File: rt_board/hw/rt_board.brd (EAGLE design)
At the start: 100 x 80 mm, 65 parts, among them IC1 MCP170333MB, IC2/L1 TLE4935L, IC3/L1 TLE4935L, IC4/L1 TLE4935L, IC5/L1 TLE4935L, Q1 8MHz, SW1 B3U-1000PM-B, SW2 B3U-1000PM-B, U1 DRV8801PWP, U2 DRV8801PWP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

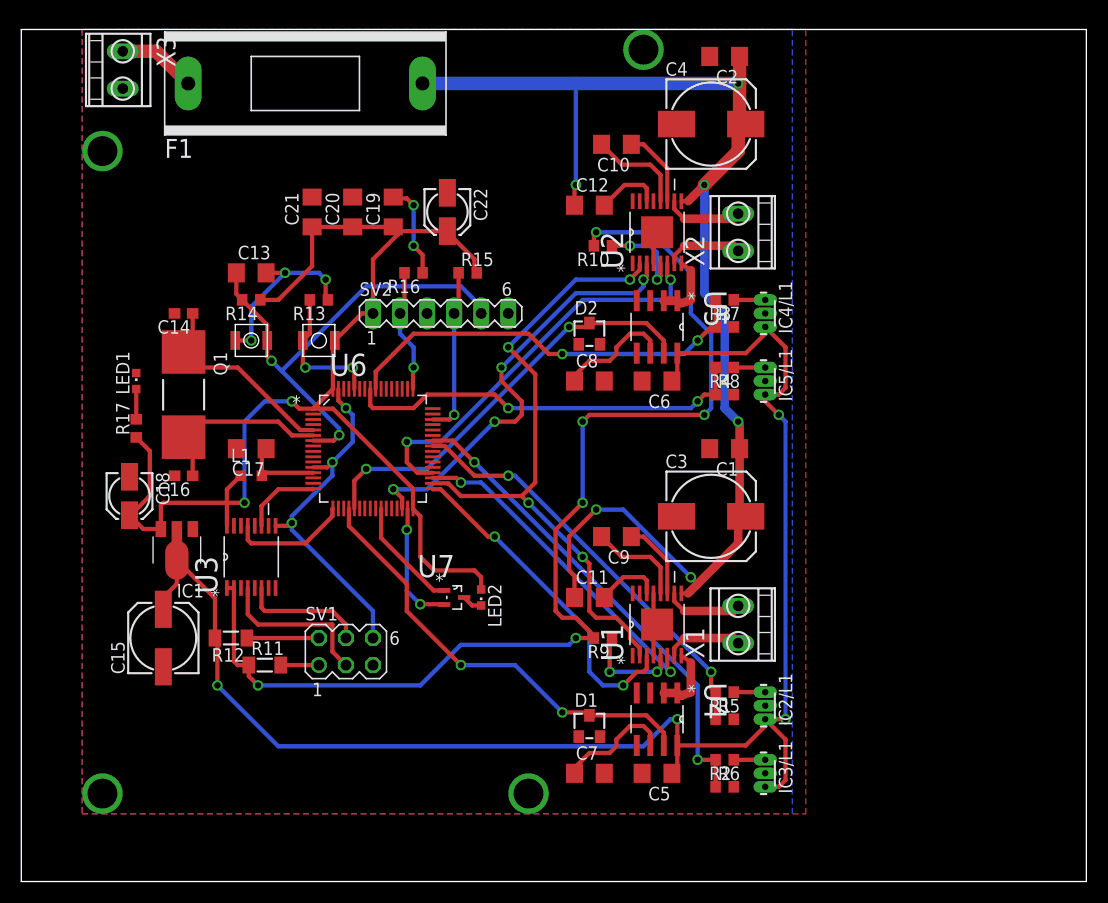
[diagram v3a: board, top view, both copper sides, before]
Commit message: board size optimized; added basic markings what is what
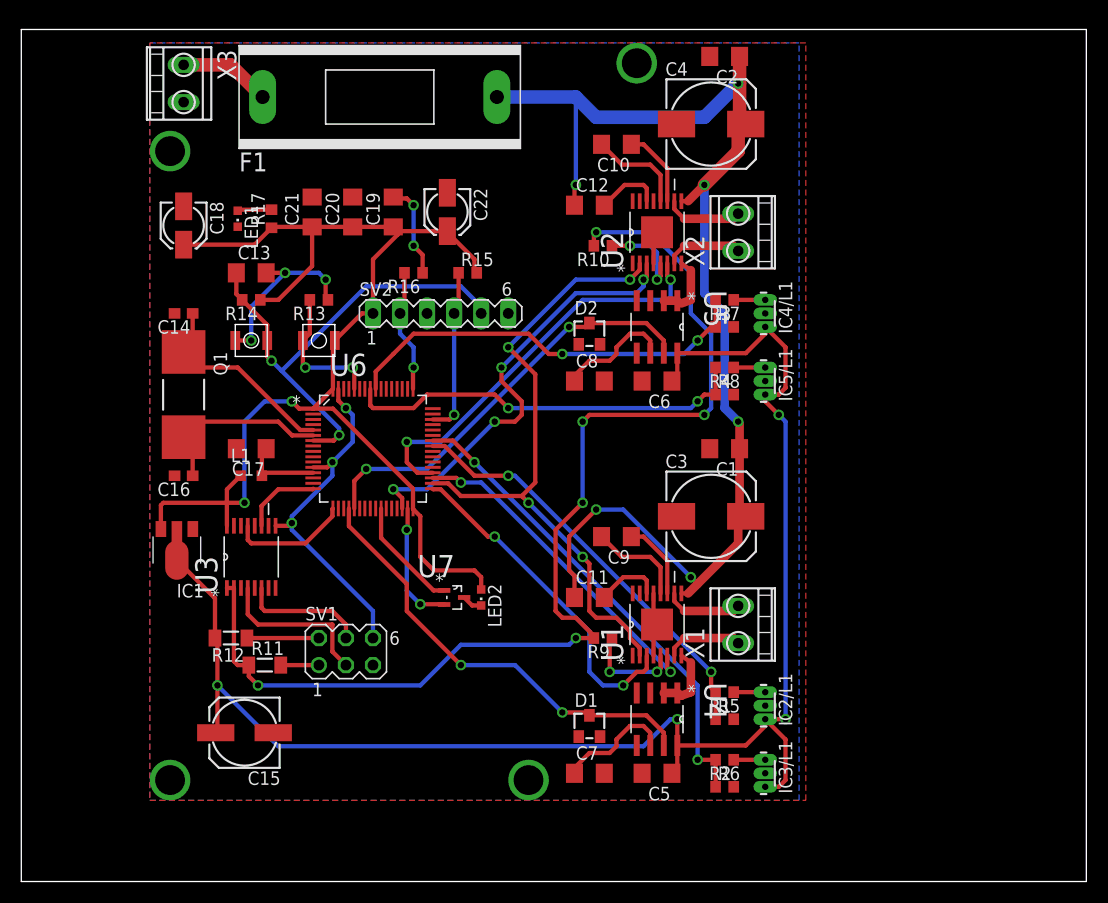
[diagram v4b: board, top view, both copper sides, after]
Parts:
- moved C18 25.9 mm to (15.2, 61.6)
- moved R17 23.4 mm to (23.5, 62.2)
- moved LED1 18.0 mm to (20.3, 62.2), turned to 180 degrees
- moved C15 11.7 mm to (21.0, 14.0), turned to 180 degrees
- moved F1 7.10 mm to (33.7, 73.7)
- moved X3 5.85 mm to (15.2, 74.9)
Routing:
- net +12V: track 124.0 -> 117.8 mm
- net N$2: track 7.40 -> 8.67 mm
- net +5V: track 117.9 -> 118.5 mm
- net +5V/1: track 143.0 -> 142.5 mm
- net 0V: vias 10 -> 14
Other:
- board text added: "+12V"
- board text added: "FASE FUSE 8A"
- board text added: "TIGER RT board v1.0.0-rc1"
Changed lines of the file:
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@@
 <wire x1="100" y1="80" x2="0" y2="80" width="0" layer="20"/>
 <wire x1="0" y1="80" x2="0" y2="0" width="0" layer="20"/>
+<text x="42.545" y="73.025" size="1.778" layer="26" rot="MR0">FASE FUSE 8A</text>
+<text x="16.51" y="71.755" size="1.778" layer="26" rot="MR90">+12V</text>
+<text x="48.895" y="13.335" size="1.778" layer="26" rot="MR0">TIGER RT board v1.0.0-rc1</text>
 </plain>
 <attributes>
@@
 <element name="C19" library="rcl" package="C1206" value="100nF" x="34.925" y="62.865" rot="R90"/>
 <element name="C22" library="rcl" package="153CLV-0405" value="4.7uF" x="40.005" y="62.865" rot="R270"/>
-<element name="C15" library="rcl" package="153CLV-0605" value="100uF" x="13.335" y="22.86" rot="R90"/>
-<element name="C18" library="rcl" package="153CLV-0405" value="4.7uF" x="10.16" y="36.195" rot="R270"/>
-<element name="X3" library="con-ptr500" package="AK550/2" value="PWR" x="9.525" y="76.2" rot="R270">
-<attribute name="OC_NEWARK" value="unknown" x="9.525" y="76.2" size="1.778" layer="27" rot="R270" display="off"/>
-<attribute name="MPN" value="" x="9.525" y="76.2" size="1.778" layer="27" rot="R270" display="off"/>
-<attribute name="MF" value="" x="9.525" y="76.2" size="1.778" layer="27" rot="R270" display="off"/>
-<attribute name="OC_FARNELL" value="unknown" x="9.525" y="76.2" size="1.778" layer="27" rot="R270" display="off"/>
-</element>
-<element name="F1" library="fuse" package="SH22" value="TF8A" x="26.67" y="74.93">
-<attribute name="OC_NEWARK" value="unknown" x="26.67" y="74.93" size="1.778" layer="27" display="off"/>
-<attribute name="MPN" value="" x="26.67" y="74.93" size="1.778" layer="27" display="off"/>
-<attribute name="MF" value="" x="26.67" y="74.93" size="1.778" layer="27" display="off"/>
-<attribute name="OC_FARNELL" value="unknown" x="26.67" y="74.93" size="1.778" layer="27" display="off"/>
+<element name="C15" library="rcl" package="153CLV-0605" value="100uF" x="20.955" y="13.97" rot="R180"/>
+<element name="C18" library="rcl" package="153CLV-0405" value="4.7uF" x="15.24" y="61.595" rot="R270"/>
+<element name="X3" library="con-ptr500" package="AK550/2" value="PWR" x="15.24" y="74.93" rot="R270">
+<attribute name="OC_NEWARK" value="unknown" x="15.24" y="74.93" size="1.778" layer="27" rot="R270" display="off"/>
+<attribute name="MPN" value="" x="15.24" y="74.93" size="1.778" layer="27" rot="R270" display="off"/>
+<attribute name="MF" value="" x="15.24" y="74.93" size="1.778" layer="27" rot="R270" display="off"/>
+<attribute name="OC_FARNELL" value="unknown" x="15.24" y="74.93" size="1.778" layer="27" rot="R270" display="off"/>
+</element>
+<element name="F1" library="fuse" package="SH22" value="TF8A" x="33.655" y="73.66">
+<attribute name="OC_NEWARK" value="unknown" x="33.655" y="73.66" size="1.778" layer="27" display="off"/>
+<attribute name="MPN" value="" x="33.655" y="73.66" size="1.778" layer="27" display="off"/>
+<attribute name="MF" value="" x="33.655" y="73.66" size="1.778" layer="27" display="off"/>
+<attribute name="OC_FARNELL" value="unknown" x="33.655" y="73.66" size="1.778" layer="27" display="off"/>
 </element>
 <element name="C20" library="rcl" package="C1206" value="100nF" x="31.115" y="62.865" rot="R90"/>
@@
 <element name="C12" library="rcl" package="C1206" value="100nF" x="53.34" y="63.5"/>
 <element name="C10" library="rcl" package="C1206" value="100nF" x="55.88" y="69.215" rot="R180"/>
-<element name="LED1" library="led" package="CHIPLED_0603" value="GREEN" x="10.795" y="46.99"/>
-<element name="R17" library="rcl" package="R0603" value="470R" x="10.795" y="42.545" rot="R90"/>
+<element name="LED1" library="led" package="CHIPLED_0603" value="GREEN" x="20.32" y="62.23" rot="R180"/>
+<element name="R17" library="rcl" package="R0603" value="470R" x="23.495" y="62.23" rot="R90"/>
 <element name="U7" library="2n7002" package="SOT65P210X110-3N" value="2N7002BKW" x="40.64" y="26.67">
 <attribute name="PACKAGE" value="SOT-3" x="40.64" y="26.67" size="1.778" layer="27" display="off"/>
@@
 <contactref element="SW2" pad="P$1"/>
 <polygon width="0.4064" layer="1">
-<vertex x="5.715" y="80.01"/>
-<vertex x="5.715" y="6.35"/>
-<vertex x="73.66" y="6.35"/>
-<vertex x="73.66" y="80.01"/>
+<vertex x="12.065" y="78.74"/>
+<vertex x="12.065" y="7.62"/>
+<vertex x="73.66" y="7.62"/>
+<vertex x="73.66" y="78.74"/>
 </polygon>
 <wire x1="36.2712" y1="35.0266" x2="36.2712" y2="33.0962" width="0.4064" layer="1"/>
@@
 <wire x1="36.195" y1="64.135" x2="35.055" y2="64.135" width="0.4064" layer="1"/>
 <wire x1="35.055" y1="64.135" x2="34.925" y2="64.265" width="0.4064" layer="1"/>
+<via x="13.97" y="68.58" extent="1-16" drill="2.8"/>
+<via x="13.97" y="9.525" extent="1-16" drill="2.8"/>
+<via x="47.625" y="9.525" extent="1-16" drill="2.8"/>
+<via x="57.785" y="76.835" extent="1-16" drill="2.8"/>
 </signal>
 <signal name="+5V">
@@
 <wire x1="34.925" y1="61.465" x2="31.115" y2="61.465" width="0.4064" layer="1"/>
 <wire x1="31.115" y1="61.465" x2="27.305" y2="61.465" width="0.4064" layer="1"/>
-<wire x1="13.106" y1="33.096" x2="11.459" y2="33.096" width="0.4064" layer="1"/>
-<wire x1="11.459" y1="33.096" x2="10.16" y2="34.395" width="0.4064" layer="1"/>
-<wire x1="10.16" y1="34.395" x2="10.265" y2="34.395" width="0.4064" layer="1"/>
-<wire x1="10.265" y1="34.395" x2="12.065" y2="36.195" width="0.4064" layer="1"/>
-<wire x1="12.065" y1="36.195" x2="12.065" y2="40.425" width="0.4064" layer="1"/>
-<wire x1="12.065" y1="40.425" x2="10.795" y2="41.695" width="0.4064" layer="1"/>
 <wire x1="13.106" y1="33.096" x2="13.106" y2="35.331" width="0.4064" layer="1"/>
 <wire x1="13.106" y1="35.331" x2="13.335" y2="35.56" width="0.4064" layer="1"/>
@@
 <via x="20.955" y="35.56" extent="1-16" drill="0.6"/>
 <wire x1="20.955" y1="35.56" x2="19.304" y2="35.56" width="0.4064" layer="1"/>
+<wire x1="27.305" y1="61.465" x2="23.495" y2="61.465" width="0.4064" layer="1"/>
+<wire x1="23.495" y1="61.465" x2="23.495" y2="61.38" width="0.4064" layer="1"/>
+<wire x1="15.24" y1="59.795" x2="21.91" y2="59.795" width="0.4064" layer="1"/>
+<wire x1="21.91" y1="59.795" x2="23.495" y2="61.38" width="0.4064" layer="1"/>
 </signal>
 <signal name="+12V">
@@
 <via x="62.865" y="28.575" extent="1-16" drill="0.6"/>
 <wire x1="62.865" y1="28.575" x2="63.5" y2="27.94" width="0.4064" layer="1"/>
-<wire x1="37.6682" y1="74.93" x2="52.07" y2="74.93" width="1.27" layer="16"/>
-<wire x1="52.07" y1="74.93" x2="67.31" y2="74.93" width="1.27" layer="16"/>
+<wire x1="44.6532" y1="73.66" x2="52.07" y2="73.66" width="1.27" layer="16"/>
+<wire x1="52.07" y1="73.66" x2="53.975" y2="71.755" width="1.27" layer="16"/>
+<wire x1="53.975" y1="71.755" x2="64.135" y2="71.755" width="1.27" layer="16"/>
+<wire x1="64.135" y1="71.755" x2="67.31" y2="74.93" width="1.27" layer="16"/>
 <wire x1="67.44" y1="74.93" x2="67.31" y2="74.93" width="0.4064" layer="1"/>
 <via x="67.31" y="74.93" extent="1-16" drill="0.6"/>
@@
 <wire x1="51.94" y1="65.275" x2="52.07" y2="65.405" width="0.4064" layer="1"/>
 <via x="52.07" y="65.405" extent="1-16" drill="0.6"/>
-<wire x1="52.07" y1="65.405" x2="52.07" y2="74.93" width="0.4064" layer="16"/>
+<wire x1="52.07" y1="65.405" x2="52.07" y2="73.66" width="0.4064" layer="16"/>
 </signal>
 <signal name="N$2">
 <contactref element="X3" pad="1"/>
 <contactref element="F1" pad="1"/>
-<wire x1="9.525" y1="77.95" x2="12.6518" y2="77.95" width="1.27" layer="1"/>
-<wire x1="12.6518" y1="77.95" x2="15.6718" y2="74.93" width="1.27" layer="1"/>
+<wire x1="15.24" y1="76.68" x2="19.6368" y2="76.68" width="1.27" layer="1"/>
+<wire x1="19.6368" y1="76.68" x2="22.6568" y2="73.66" width="1.27" layer="1"/>
 </signal>
 <signal name="N$5">
@@
 <contactref element="IC1" pad="2@1"/>
 <contactref element="C15" pad="+"/>
-<wire x1="13.335" y1="25.56" x2="13.335" y2="26.67" width="0.4064" layer="1"/>
-<wire x1="13.335" y1="26.67" x2="14.605" y2="27.94" width="0.4064" layer="1"/>
-<wire x1="14.605" y1="27.94" x2="14.605" y2="30.175" width="0.4064" layer="1"/>
 <wire x1="18.185" y1="22.86" x2="18.185" y2="26.595" width="0.4064" layer="1"/>
 <wire x1="18.185" y1="26.595" x2="14.605" y2="30.175" width="0.4064" layer="1"/>
@@
 <wire x1="18.415" y1="18.415" x2="18.415" y2="22.63" width="0.4064" layer="1"/>
 <wire x1="18.415" y1="22.63" x2="18.185" y2="22.86" width="0.4064" layer="1"/>
+<wire x1="18.255" y1="13.97" x2="18.415" y2="13.97" width="0.4064" layer="1"/>
+<wire x1="18.415" y1="13.97" x2="18.415" y2="18.415" width="0.4064" layer="1"/>
 </signal>
 <signal name="N$11">
@@
 <contactref element="LED1" pad="A"/>
 <contactref element="R17" pad="2"/>
-<wire x1="10.795" y1="43.395" x2="10.795" y2="46.24" width="0.4064" layer="1"/>
+<wire x1="23.495" y1="63.08" x2="20.32" y2="63.08" width="0.4064" layer="1"/>
+<wire x1="20.32" y1="63.08" x2="20.32" y2="62.98" width="0.4064" layer="1"/>
 </signal>
 <signal name="N$44">
@@
 <signal name="N$50">
 <polygon width="0.4064" layer="16">
-<vertex x="5.715" y="80.01"/>
-<vertex x="5.715" y="6.35"/>
-<vertex x="72.39" y="6.35"/>
-<vertex x="72.39" y="80.01"/>
+<vertex x="12.065" y="78.74"/>
+<vertex x="12.065" y="7.62"/>
+<vertex x="73.025" y="7.62"/>
+<vertex x="73.025" y="78.74"/>
 </polygon>
 </signal>
-<signal name="N$1">
-<via x="7.62" y="8.255" extent="1-16" drill="2.8"/>
-</signal>
-<signal name="N$51">
-<via x="47.625" y="8.255" extent="1-16" drill="2.8"/>
-</signal>
-<signal name="N$52">
-<via x="58.42" y="78.105" extent="1-16" drill="2.8"/>
-</signal>
-<signal name="N$53">
-<via x="7.62" y="68.58" extent="1-16" drill="2.8"/>
-</signal>
 </signals>
